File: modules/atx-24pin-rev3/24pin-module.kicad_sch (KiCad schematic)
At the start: 64 parts, among them J1 TO-HUB, J2 TO-HUB-PWR, J3 ATX-24 PSU, J4 ATX-24 MB, J5 USB-C 2.0, J6 TO-HUB-STACK, SW1 BOOT, SW2 RESET, U1 ESP32-C6-MINI-1-N4, U10 INA228, U11 INA228, U12 INA228, U13 INA228, U2 TJA1051T/3, U3 LP5907MFX-3.3, U5 TPS2121RUXR, U612V INA181A2IDBVR, U65V INA181A2IDBVR, U712V TLV7011DBVR, U75V TLV7011DBVR

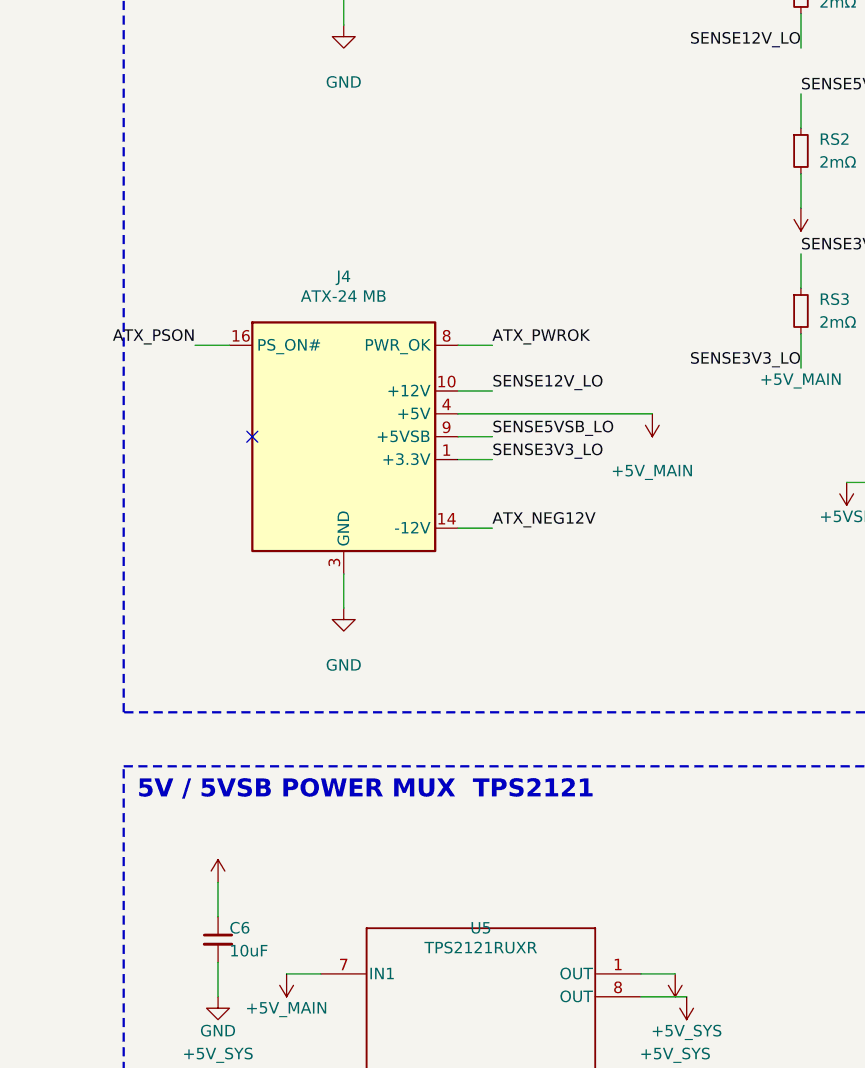
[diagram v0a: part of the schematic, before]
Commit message: Task 9: blade interface on main boards — J4/J_OUT* -> Keystone 3586 clips + J_SIG (SS2.8 v1.4.0)
24pin-rev3 hand-splice: TB1..TB9 per the ratified rail split + 2x5 J_SIG
(PS_ON#/PWR_OK/-12V/GND; pins 5-10 reserved — NO remote-sense net exists on
J4, verified not invented); EPS/PCIe = generator edits + regen (TB per-cable
3+3 / 2+2 on /SENSEC*_LO + GND). Modeled-delta assertions PASS all 4 boards
(exactly J_OUT/J4 out, TB/J_SIG in; inventory otherwise byte-identical);
ERC byte-identical on EPS/PCIe, 24pin +4 benign warnings/errors unchanged;
BOMs updated (C238113 in, Mini-Fit-out rows gone). Rev -> BETA-2. Two real
shared-code bugs fixed (auto_io vertical-pin heuristic; title_block comment4
arity). Sense-return NOT added (owner box (e) open — provision comments).
12VHPWR + all inputs untouched. 24pin pre-existing missing_lib_symbol x4 ->
FOLLOWUPS.

Co-Authored-By: Claude Fable 5 <noreply@anthropic.com>
Claude-Session: https://claude.ai/code/session_01LvfqcnEeuin2oyJQw548EX
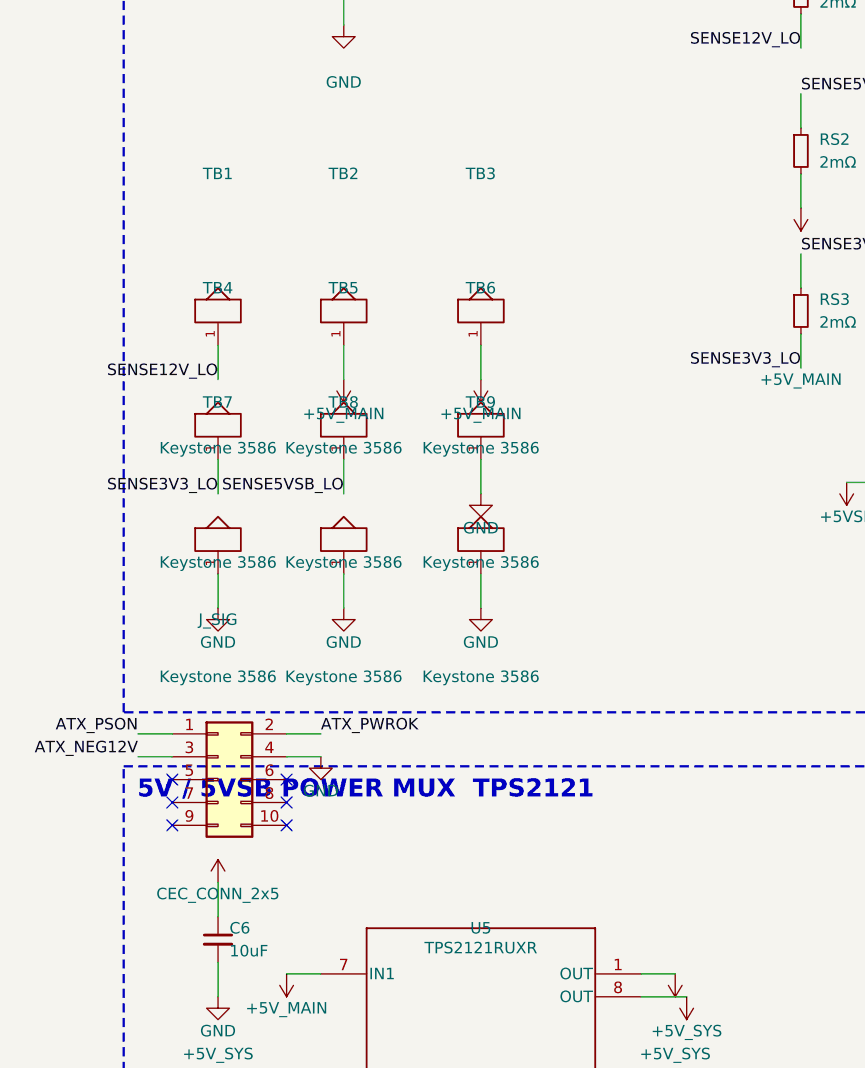
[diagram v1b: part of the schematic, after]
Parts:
- removed J4: ATX-24 MB, cec-Connector_Molex:Molex_Mini-Fit_Jr_5569-24A2_2x12_P4.20mm_Horizontal, symbol cec:CEC_ATX_24
- added J_SIG: CEC_CONN_2x5, cec-Connector_PinHeader_2.54mm:PinHeader_2x05_P2.54mm_Vertical, symbol cec:CEC_CONN_2x5
- added TB1, TB2, TB3, TB4, TB5, TB6, TB7, TB8, TB9: Keystone 3586, cec-Connector_Blade:Keystone_3586_SMD_Universal_Blade_Clip, symbol cec-vendor:Keystone_3586_Blade_Clip
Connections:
- net +3V3: now also J_SIG.4 (Pin_4), TB6.1, TB7.1, TB8.1, TB9.1
- net +5V_MAIN: now also TB2.1, TB3.1
- net ATX_NEG12V: now also J_SIG.3 (Pin_3)
- net ATX_PSON: now also J_SIG.1 (Pin_1)
- net ATX_PWROK: now also J_SIG.2 (Pin_2)
- net SENSE12V_LO: now also TB1.1
- net SENSE3V3_LO: now also TB4.1
- net SENSE5VSB_LO: now also TB5.1
- no-connect marks 34 -> 39

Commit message: WIP snapshot: INA238 ruling application in progress (spec v1.5.0 + 24pin-rev3 swap, verification pending; durability)
Co-Authored-By: Claude Fable 5 <noreply@anthropic.com>
Claude-Session: https://claude.ai/code/session_01LvfqcnEeuin2oyJQw548EX
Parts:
- U10, U11, U12, U13: value INA228 -> INA238; LCSC (none) -> C2868250; MPN (none) -> INA238AIDGSR; Manufacturer (none) -> Texas Instruments
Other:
- note added: "RAIL SENSING 4x INA238"
- note removed: "RAIL SENSING 4x INA228"
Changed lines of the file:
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@@
 		(fill (type none))
 	)
-	(text "RAIL SENSING  4x INA228"
+	(text "RAIL SENSING  4x INA238"
 		(exclude_from_sim no)
 		(at 135.5 25.5 0)
@@
 		(fields_autoplaced yes)
 		(property "Reference" "U10" (at 151.52 49.61 0) (effects (font (size 1.27 1.27)) (justify right)))
-		(property "Value" "INA228" (at 151.52 52.11 0) (effects (font (size 1.27 1.27)) (justify right)))
+		(property "Value" "INA238" (at 151.52 52.11 0) (effects (font (size 1.27 1.27)) (justify right)))
 		(property "Footprint" "cec-Package_SO:VSSOP-10_3x3mm_P0.5mm" (at 160.02 54.61 0) (effects (font (size 1.27 1.27)) (hide yes)))
 		(property "Datasheet" "" (at 160.02 54.61 0) (effects (font (size 1.27 1.27)) (hide yes)))
+		(property "Manufacturer" "Texas Instruments" (at 160.02 54.61 0) (effects (font (size 1.27 1.27)) (hide yes)))
+		(property "MPN" "INA238AIDGSR" (at 160.02 54.61 0) (effects (font (size 1.27 1.27)) (hide yes)))
+		(property "LCSC" "C2868250" (at 160.02 54.61 0) (effects (font (size 1.27 1.27)) (hide yes)))
 		(pin "8")
 		(pin "10")
@@
 		(fields_autoplaced yes)
 		(property "Reference" "U11" (at 150.25 80.09 0) (effects (font (size 1.27 1.27)) (justify right)))
-		(property "Value" "INA228" (at 150.25 82.29 0) (effects (font (size 1.27 1.27)) (justify right)))
+		(property "Value" "INA238" (at 150.25 82.29 0) (effects (font (size 1.27 1.27)) (justify right)))
 		(property "Footprint" "cec-Package_SO:VSSOP-10_3x3mm_P0.5mm" (at 160.02 85.09 0) (effects (font (size 1.27 1.27)) (hide yes)))
 		(property "Datasheet" "" (at 160.02 85.09 0) (effects (font (size 1.27 1.27)) (hide yes)))
+		(property "Manufacturer" "Texas Instruments" (at 160.02 85.09 0) (effects (font (size 1.27 1.27)) (hide yes)))
+		(property "MPN" "INA238AIDGSR" (at 160.02 85.09 0) (effects (font (size 1.27 1.27)) (hide yes)))
+		(property "LCSC" "C2868250" (at 160.02 85.09 0) (effects (font (size 1.27 1.27)) (hide yes)))
 		(pin "8")
 		(pin "10")
@@
 		(fields_autoplaced yes)
 		(property "Reference" "U12" (at 151.52 110.57 0) (effects (font (size 1.27 1.27)) (justify right)))
-		(property "Value" "INA228" (at 151.52 113.07 0) (effects (font (size 1.27 1.27)) (justify right)))
+		(property "Value" "INA238" (at 151.52 113.07 0) (effects (font (size 1.27 1.27)) (justify right)))
 		(property "Footprint" "cec-Package_SO:VSSOP-10_3x3mm_P0.5mm" (at 160.02 115.57 0) (effects (font (size 1.27 1.27)) (hide yes)))
 		(property "Datasheet" "" (at 160.02 115.57 0) (effects (font (size 1.27 1.27)) (hide yes)))
+		(property "Manufacturer" "Texas Instruments" (at 160.02 115.57 0) (effects (font (size 1.27 1.27)) (hide yes)))
+		(property "MPN" "INA238AIDGSR" (at 160.02 115.57 0) (effects (font (size 1.27 1.27)) (hide yes)))
+		(property "LCSC" "C2868250" (at 160.02 115.57 0) (effects (font (size 1.27 1.27)) (hide yes)))
 		(pin "8")
 		(pin "10")
@@
 		(fields_autoplaced yes)
 		(property "Reference" "U13" (at 201.05 49.61 0) (effects (font (size 1.27 1.27)) (justify right)))
-		(property "Value" "INA228" (at 201.05 51.81 0) (effects (font (size 1.27 1.27)) (justify right)))
+		(property "Value" "INA238" (at 201.05 51.81 0) (effects (font (size 1.27 1.27)) (justify right)))
 		(property "Footprint" "cec-Package_SO:VSSOP-10_3x3mm_P0.5mm" (at 209.55 54.61 0) (effects (font (size 1.27 1.27)) (hide yes)))
 		(property "Datasheet" "" (at 209.55 54.61 0) (effects (font (size 1.27 1.27)) (hide yes)))
+		(property "Manufacturer" "Texas Instruments" (at 209.55 54.61 0) (effects (font (size 1.27 1.27)) (hide yes)))
+		(property "MPN" "INA238AIDGSR" (at 209.55 54.61 0) (effects (font (size 1.27 1.27)) (hide yes)))
+		(property "LCSC" "C2868250" (at 209.55 54.61 0) (effects (font (size 1.27 1.27)) (hide yes)))
 		(pin "8")
 		(pin "10")

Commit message: WIP snapshot: iteration-5 main-board clip swap in flight (durability)
Co-Authored-By: Claude Fable 5 <noreply@anthropic.com>
Claude-Session: https://claude.ai/code/session_01LvfqcnEeuin2oyJQw548EX
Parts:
- TB1: value Keystone 3586 -> Keystone 3557; footprint cec-Connector_Blade:Keystone_3586_SMD_Universal_Blade_Clip -> cec-Connector_Blade:Keystone_3557_THT_Universal_Clip_TopEntry; LCSC C238113 -> C3205403; MPN 3586 -> 3557; Note Output daughterboard blade clip, ratified joint 12V (spec Sec 2.8 v1.4.0); mates with the TE 63849-1 tab on the daughterboard side. -> Output daughterboard blade clip, ratified joint 12V (spec Sec 2.8 v1.4.0); mates with the TE 63849-1 tab on the daughterboard side. [2026-07-05 iteration 5: clip part swapped Keystone 3586 (SMD) -> Keystone 3557 bare top-entry clip (THT, UL 30A@500VAC, catalog M55 p.41; LCSC carriage: 3557-10/C3205403 in the fuse-holder category, variant UNVERIFIED -- DigiKey/Mouser carry 3557 directly, consigned fallback; 3586 stays vendored as the SMD fallback pending the OQ-86 sample). Rotated: slot axis perpendicular to the daughterboard wall line, legs ALONG the clip row (3.4mm pitch, verified from the catalog mounting details). Mates the TE 63951-1 right-angle tab descending blade-down from the daughterboard -- see docs/standard-tier-review/blade-fit-check-2026-07-04.md addenda 3-5.]
- TB2: value Keystone 3586 -> Keystone 3557; footprint cec-Connector_Blade:Keystone_3586_SMD_Universal_Blade_Clip -> cec-Connector_Blade:Keystone_3557_THT_Universal_Clip_TopEntry; LCSC C238113 -> C3205403; MPN 3586 -> 3557; Note Output daughterboard blade clip, ratified joint 5V (1 of 2) (spec Sec 2.8 v1.4.0); mates with the TE 63849-1 tab on the daughterboard side. -> Output daughterboard blade clip, ratified joint 5V (1 of 2) (spec Sec 2.8 v1.4.0); mates with the TE 63849-1 tab on the daughterboard side. [2026-07-05 iteration 5: clip part swapped Keystone 3586 (SMD) -> Keystone 3557 bare top-entry clip (THT, UL 30A@500VAC, catalog M55 p.41; LCSC carriage: 3557-10/C3205403 in the fuse-holder category, variant UNVERIFIED -- DigiKey/Mouser carry 3557 directly, consigned fallback; 3586 stays vendored as the SMD fallback pending the OQ-86 sample). Rotated: slot axis perpendicular to the daughterboard wall line, legs ALONG the clip row (3.4mm pitch, verified from the catalog mounting details). Mates the TE 63951-1 right-angle tab descending blade-down from the daughterboard -- see docs/standard-tier-review/blade-fit-check-2026-07-04.md addenda 3-5.]
- TB3: value Keystone 3586 -> Keystone 3557; footprint cec-Connector_Blade:Keystone_3586_SMD_Universal_Blade_Clip -> cec-Connector_Blade:Keystone_3557_THT_Universal_Clip_TopEntry; LCSC C238113 -> C3205403; MPN 3586 -> 3557; Note Output daughterboard blade clip, ratified joint 5V (2 of 2) (spec Sec 2.8 v1.4.0); mates with the TE 63849-1 tab on the daughterboard side. -> Output daughterboard blade clip, ratified joint 5V (2 of 2) (spec Sec 2.8 v1.4.0); mates with the TE 63849-1 tab on the daughterboard side. [2026-07-05 iteration 5: clip part swapped Keystone 3586 (SMD) -> Keystone 3557 bare top-entry clip (THT, UL 30A@500VAC, catalog M55 p.41; LCSC carriage: 3557-10/C3205403 in the fuse-holder category, variant UNVERIFIED -- DigiKey/Mouser carry 3557 directly, consigned fallback; 3586 stays vendored as the SMD fallback pending the OQ-86 sample). Rotated: slot axis perpendicular to the daughterboard wall line, legs ALONG the clip row (3.4mm pitch, verified from the catalog mounting details). Mates the TE 63951-1 right-angle tab descending blade-down from the daughterboard -- see docs/standard-tier-review/blade-fit-check-2026-07-04.md addenda 3-5.]
- TB4: value Keystone 3586 -> Keystone 3557; footprint cec-Connector_Blade:Keystone_3586_SMD_Universal_Blade_Clip -> cec-Connector_Blade:Keystone_3557_THT_Universal_Clip_TopEntry; LCSC C238113 -> C3205403; MPN 3586 -> 3557; Note Output daughterboard blade clip, ratified joint 3.3V (spec Sec 2.8 v1.4.0); mates with the TE 63849-1 tab on the daughterboard side. -> Output daughterboard blade clip, ratified joint 3.3V (spec Sec 2.8 v1.4.0); mates with the TE 63849-1 tab on the daughterboard side. [2026-07-05 iteration 5: clip part swapped Keystone 3586 (SMD) -> Keystone 3557 bare top-entry clip (THT, UL 30A@500VAC, catalog M55 p.41; LCSC carriage: 3557-10/C3205403 in the fuse-holder category, variant UNVERIFIED -- DigiKey/Mouser carry 3557 directly, consigned fallback; 3586 stays vendored as the SMD fallback pending the OQ-86 sample). Rotated: slot axis perpendicular to the daughterboard wall line, legs ALONG the clip row (3.4mm pitch, verified from the catalog mounting details). Mates the TE 63951-1 right-angle tab descending blade-down from the daughterboard -- see docs/standard-tier-review/blade-fit-check-2026-07-04.md addenda 3-5.]
- TB5: value Keystone 3586 -> Keystone 3557; footprint cec-Connector_Blade:Keystone_3586_SMD_Universal_Blade_Clip -> cec-Connector_Blade:Keystone_3557_THT_Universal_Clip_TopEntry; LCSC C238113 -> C3205403; MPN 3586 -> 3557; Note Output daughterboard blade clip, ratified joint 5VSB (spec Sec 2.8 v1.4.0); mates with the TE 63849-1 tab on the daughterboard side. -> Output daughterboard blade clip, ratified joint 5VSB (spec Sec 2.8 v1.4.0); mates with the TE 63849-1 tab on the daughterboard side. [2026-07-05 iteration 5: clip part swapped Keystone 3586 (SMD) -> Keystone 3557 bare top-entry clip (THT, UL 30A@500VAC, catalog M55 p.41; LCSC carriage: 3557-10/C3205403 in the fuse-holder category, variant UNVERIFIED -- DigiKey/Mouser carry 3557 directly, consigned fallback; 3586 stays vendored as the SMD fallback pending the OQ-86 sample). Rotated: slot axis perpendicular to the daughterboard wall line, legs ALONG the clip row (3.4mm pitch, verified from the catalog mounting details). Mates the TE 63951-1 right-angle tab descending blade-down from the daughterboard -- see docs/standard-tier-review/blade-fit-check-2026-07-04.md addenda 3-5.]
- TB6: value Keystone 3586 -> Keystone 3557; footprint cec-Connector_Blade:Keystone_3586_SMD_Universal_Blade_Clip -> cec-Connector_Blade:Keystone_3557_THT_Universal_Clip_TopEntry; LCSC C238113 -> C3205403; MPN 3586 -> 3557; Note Output daughterboard blade clip, ratified joint GND (1 of 4) (spec Sec 2.8 v1.4.0); mates with the TE 63849-1 tab on the daughterboard side. -> Output daughterboard blade clip, ratified joint GND (1 of 4) (spec Sec 2.8 v1.4.0); mates with the TE 63849-1 tab on the daughterboard side. [2026-07-05 iteration 5: clip part swapped Keystone 3586 (SMD) -> Keystone 3557 bare top-entry clip (THT, UL 30A@500VAC, catalog M55 p.41; LCSC carriage: 3557-10/C3205403 in the fuse-holder category, variant UNVERIFIED -- DigiKey/Mouser carry 3557 directly, consigned fallback; 3586 stays vendored as the SMD fallback pending the OQ-86 sample). Rotated: slot axis perpendicular to the daughterboard wall line, legs ALONG the clip row (3.4mm pitch, verified from the catalog mounting details). Mates the TE 63951-1 right-angle tab descending blade-down from the daughterboard -- see docs/standard-tier-review/blade-fit-check-2026-07-04.md addenda 3-5.]
- TB7: value Keystone 3586 -> Keystone 3557; footprint cec-Connector_Blade:Keystone_3586_SMD_Universal_Blade_Clip -> cec-Connector_Blade:Keystone_3557_THT_Universal_Clip_TopEntry; LCSC C238113 -> C3205403; MPN 3586 -> 3557; Note Output daughterboard blade clip, ratified joint GND (2 of 4) (spec Sec 2.8 v1.4.0); mates with the TE 63849-1 tab on the daughterboard side. -> Output daughterboard blade clip, ratified joint GND (2 of 4) (spec Sec 2.8 v1.4.0); mates with the TE 63849-1 tab on the daughterboard side. [2026-07-05 iteration 5: clip part swapped Keystone 3586 (SMD) -> Keystone 3557 bare top-entry clip (THT, UL 30A@500VAC, catalog M55 p.41; LCSC carriage: 3557-10/C3205403 in the fuse-holder category, variant UNVERIFIED -- DigiKey/Mouser carry 3557 directly, consigned fallback; 3586 stays vendored as the SMD fallback pending the OQ-86 sample). Rotated: slot axis perpendicular to the daughterboard wall line, legs ALONG the clip row (3.4mm pitch, verified from the catalog mounting details). Mates the TE 63951-1 right-angle tab descending blade-down from the daughterboard -- see docs/standard-tier-review/blade-fit-check-2026-07-04.md addenda 3-5.]
- TB8: value Keystone 3586 -> Keystone 3557; footprint cec-Connector_Blade:Keystone_3586_SMD_Universal_Blade_Clip -> cec-Connector_Blade:Keystone_3557_THT_Universal_Clip_TopEntry; LCSC C238113 -> C3205403; MPN 3586 -> 3557; Note Output daughterboard blade clip, ratified joint GND (3 of 4) (spec Sec 2.8 v1.4.0); mates with the TE 63849-1 tab on the daughterboard side. -> Output daughterboard blade clip, ratified joint GND (3 of 4) (spec Sec 2.8 v1.4.0); mates with the TE 63849-1 tab on the daughterboard side. [2026-07-05 iteration 5: clip part swapped Keystone 3586 (SMD) -> Keystone 3557 bare top-entry clip (THT, UL 30A@500VAC, catalog M55 p.41; LCSC carriage: 3557-10/C3205403 in the fuse-holder category, variant UNVERIFIED -- DigiKey/Mouser carry 3557 directly, consigned fallback; 3586 stays vendored as the SMD fallback pending the OQ-86 sample). Rotated: slot axis perpendicular to the daughterboard wall line, legs ALONG the clip row (3.4mm pitch, verified from the catalog mounting details). Mates the TE 63951-1 right-angle tab descending blade-down from the daughterboard -- see docs/standard-tier-review/blade-fit-check-2026-07-04.md addenda 3-5.]
- TB9: value Keystone 3586 -> Keystone 3557; footprint cec-Connector_Blade:Keystone_3586_SMD_Universal_Blade_Clip -> cec-Connector_Blade:Keystone_3557_THT_Universal_Clip_TopEntry; LCSC C238113 -> C3205403; MPN 3586 -> 3557; Note Output daughterboard blade clip, ratified joint GND (4 of 4) (spec Sec 2.8 v1.4.0); mates with the TE 63849-1 tab on the daughterboard side. -> Output daughterboard blade clip, ratified joint GND (4 of 4) (spec Sec 2.8 v1.4.0); mates with the TE 63849-1 tab on the daughterboard side. [2026-07-05 iteration 5: clip part swapped Keystone 3586 (SMD) -> Keystone 3557 bare top-entry clip (THT, UL 30A@500VAC, catalog M55 p.41; LCSC carriage: 3557-10/C3205403 in the fuse-holder category, variant UNVERIFIED -- DigiKey/Mouser carry 3557 directly, consigned fallback; 3586 stays vendored as the SMD fallback pending the OQ-86 sample). Rotated: slot axis perpendicular to the daughterboard wall line, legs ALONG the clip row (3.4mm pitch, verified from the catalog mounting details). Mates the TE 63951-1 right-angle tab descending blade-down from the daughterboard -- see docs/standard-tier-review/blade-fit-check-2026-07-04.md addenda 3-5.]

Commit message: Daughterboard iteration 7 LANDED: TE 63969-1 receptacles, owner-ratified counts, orientation checker-proven
- Boards: atx24 61.0x21.4 @4.2mm/10 tabs; eps 28.5x20.0 @4.7/6; pcie 31.0x20.0 @5.2/6 (grows: +2 ratified joints outweigh the pitch win — honest number)
- Orientation proven from the rev-E drawing (memo addendum 7 F.1) + structural checker assertion (hole pair perpendicular to row, plan-congruent with the blade's leg holes, per position)
- atx24 rail allocation at 18.32A/joint: 12V 1 / 5V 2 / 3V3 2 (the gained joint; was 95% FAIL) / 5VSB 1 / GND 4 @127.2% hairline — honest 10
- Receptacle depth un-dimensioned on rev E: sample-gated 3.4-3.7 est w/ explicit >4.0mm => atx24-falls-back-to-6.3 gate in the checker
- Main boards: TB property swaps to TE 63969-1/C2961150 + ratified adds netlist-verified post-shunt (24pin TB10, pcie +2/cable); STALE Keystone-3586 BOM lines from Task 9 fixed
- Coordinator re-verified: ERC 0 x3 + DRC 0/0 x3 daughterboards; checker 113 OKs; 24pin-rev3 ERC = 1 pre-existing pin_not_driven only
- New sample items: detent hole ~0.5mm above receptacle top (retention friction-only?), gang insertion <=26N LIF / <=44N std per joint

Co-Authored-By: Claude Fable 5 <noreply@anthropic.com>
Claude-Session: https://claude.ai/code/session_01LvfqcnEeuin2oyJQw548EX
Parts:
- added TB10: TE 63969-1, cec-Connector_Blade:TE_63969_FASTON_Receptacle_250_Vertical_THT, symbol cec-vendor:Keystone_3586_Blade_Clip
- TB1: value Keystone 3557 -> TE 63969-1; footprint cec-Connector_Blade:Keystone_3557_THT_Universal_Clip_TopEntry -> cec-Connector_Blade:TE_63969_FASTON_Receptacle_250_Vertical_THT; LCSC C3205403 -> C2961150; MPN 3557 -> 63969-1; Manufacturer Keystone Electronics Corp. -> TE Connectivity; Note Output daughterboard blade clip, ratified joint 12V (spec Sec 2.8 v1.4.0); mates with the TE 63849-1 tab on the daughterboard side. [2026-07-05 iteration 5: clip part swapped Keystone 3586 (SMD) -> Keystone 3557 bare top-entry clip (THT, UL 30A@500VAC, catalog M55 p.41; LCSC carriage: 3557-10/C3205403 in the fuse-holder category, variant UNVERIFIED -- DigiKey/Mouser carry 3557 directly, consigned fallback; 3586 stays vendored as the SMD fallback pending the OQ-86 sample). Rotated: slot axis perpendicular to the daughterboard wall line, legs ALONG the clip row (3.4mm pitch, verified from the catalog mounting details). Mates the TE 63951-1 right-angle tab descending blade-down from the daughterboard -- see docs/standard-tier-review/blade-fit-check-2026-07-04.md addenda 3-5.] -> Output daughterboard blade clip, ratified joint 12V (spec Sec 2.8 v1.4.0); mates with the TE 63849-1 tab on the daughterboard side. [2026-07-05 iteration 5: clip part swapped Keystone 3586 (SMD) -> Keystone 3557 bare top-entry clip (THT, UL 30A@500VAC, catalog M55 p.41; LCSC carriage: 3557-10/C3205403 in the fuse-holder category, variant UNVERIFIED -- DigiKey/Mouser carry 3557 directly, consigned fallback; 3586 stays vendored as the SMD fallback pending the OQ-86 sample). Rotated: slot axis perpendicular to the daughterboard wall line, legs ALONG the clip row (3.4mm pitch, verified from the catalog mounting details). Mates the TE 63951-1 right-angle tab descending blade-down from the daughterboard -- see docs/standard-tier-review/blade-fit-check-2026-07-04.md addenda 3-5.] [2026-07-06 iteration 7: mate swapped Keystone 3557 -> TE 63969-1 FASTON .250 PCB receptacle (owner-ratified; the DESIGNED mate for the 63951-1 blade -- 0.81mm thickness at its design centre per rev-E dwg note 3, ve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
- TB2: value Keystone 3557 -> TE 63969-1; footprint cec-Connector_Blade:Keystone_3557_THT_Universal_Clip_TopEntry -> cec-Connector_Blade:TE_63969_FASTON_Receptacle_250_Vertical_THT; LCSC C3205403 -> C2961150; MPN 3557 -> 63969-1; Manufacturer Keystone Electronics Corp. -> TE Connectivity; Note Output daughterboard blade clip, ratified joint 5V (1 of 2) (spec Sec 2.8 v1.4.0); mates with the TE 63849-1 tab on the daughterboard side. [2026-07-05 iteration 5: clip part swapped Keystone 3586 (SMD) -> Keystone 3557 bare top-entry clip (THT, UL 30A@500VAC, catalog M55 p.41; LCSC carriage: 3557-10/C3205403 in the fuse-holder category, variant UNVERIFIED -- DigiKey/Mouser carry 3557 directly, consigned fallback; 3586 stays vendored as the SMD fallback pending the OQ-86 sample). Rotated: slot axis perpendicular to the daughterboard wall line, legs ALONG the clip row (3.4mm pitch, verified from the catalog mounting details). Mates the TE 63951-1 right-angle tab descending blade-down from the daughterboard -- see docs/standard-tier-review/blade-fit-check-2026-07-04.md addenda 3-5.] -> Output daughterboard blade clip, ratified joint 5V (1 of 2) (spec Sec 2.8 v1.4.0); mates with the TE 63849-1 tab on the daughterboard side. [2026-07-05 iteration 5: clip part swapped Keystone 3586 (SMD) -> Keystone 3557 bare top-entry clip (THT, UL 30A@500VAC, catalog M55 p.41; LCSC carriage: 3557-10/C3205403 in the fuse-holder category, variant UNVERIFIED -- DigiKey/Mouser carry 3557 directly, consigned fallback; 3586 stays vendored as the SMD fallback pending the OQ-86 sample). Rotated: slot axis perpendicular to the daughterboard wall line, legs ALONG the clip row (3.4mm pitch, verified from the catalog mounting details). Mates the TE 63951-1 right-angle tab descending blade-down from the daughterboard -- see docs/standard-tier-review/blade-fit-check-2026-07-04.md addenda 3-5.] [2026-07-06 iteration 7: mate swapped Keystone 3557 -> TE 63969-1 FASTON .250 PCB receptacle (owner-ratified; the DESIGNED mate for the 63951-1 blade -- 0.81mm thickness at its design centre per rev-E dwg no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
- TB3: value Keystone 3557 -> TE 63969-1; footprint cec-Connector_Blade:Keystone_3557_THT_Universal_Clip_TopEntry -> cec-Connector_Blade:TE_63969_FASTON_Receptacle_250_Vertical_THT; LCSC C3205403 -> C2961150; MPN 3557 -> 63969-1; Manufacturer Keystone Electronics Corp. -> TE Connectivity; Note Output daughterboard blade clip, ratified joint 5V (2 of 2) (spec Sec 2.8 v1.4.0); mates with the TE 63849-1 tab on the daughterboard side. [2026-07-05 iteration 5: clip part swapped Keystone 3586 (SMD) -> Keystone 3557 bare top-entry clip (THT, UL 30A@500VAC, catalog M55 p.41; LCSC carriage: 3557-10/C3205403 in the fuse-holder category, variant UNVERIFIED -- DigiKey/Mouser carry 3557 directly, consigned fallback; 3586 stays vendored as the SMD fallback pending the OQ-86 sample). Rotated: slot axis perpendicular to the daughterboard wall line, legs ALONG the clip row (3.4mm pitch, verified from the catalog mounting details). Mates the TE 63951-1 right-angle tab descending blade-down from the daughterboard -- see docs/standard-tier-review/blade-fit-check-2026-07-04.md addenda 3-5.] -> Output daughterboard blade clip, ratified joint 5V (2 of 2) (spec Sec 2.8 v1.4.0); mates with the TE 63849-1 tab on the daughterboard side. [2026-07-05 iteration 5: clip part swapped Keystone 3586 (SMD) -> Keystone 3557 bare top-entry clip (THT, UL 30A@500VAC, catalog M55 p.41; LCSC carriage: 3557-10/C3205403 in the fuse-holder category, variant UNVERIFIED -- DigiKey/Mouser carry 3557 directly, consigned fallback; 3586 stays vendored as the SMD fallback pending the OQ-86 sample). Rotated: slot axis perpendicular to the daughterboard wall line, legs ALONG the clip row (3.4mm pitch, verified from the catalog mounting details). Mates the TE 63951-1 right-angle tab descending blade-down from the daughterboard -- see docs/standard-tier-review/blade-fit-check-2026-07-04.md addenda 3-5.] [2026-07-06 iteration 7: mate swapped Keystone 3557 -> TE 63969-1 FASTON .250 PCB receptacle (owner-ratified; the DESIGNED mate for the 63951-1 blade -- 0.81mm thickness at its design centre per rev-E dwg no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
- TB4: value Keystone 3557 -> TE 63969-1; footprint cec-Connector_Blade:Keystone_3557_THT_Universal_Clip_TopEntry -> cec-Connector_Blade:TE_63969_FASTON_Receptacle_250_Vertical_THT; LCSC C3205403 -> C2961150; MPN 3557 -> 63969-1; Manufacturer Keystone Electronics Corp. -> TE Connectivity; Note Output daughterboard blade clip, ratified joint 3.3V (spec Sec 2.8 v1.4.0); mates with the TE 63849-1 tab on the daughterboard side. [2026-07-05 iteration 5: clip part swapped Keystone 3586 (SMD) -> Keystone 3557 bare top-entry clip (THT, UL 30A@500VAC, catalog M55 p.41; LCSC carriage: 3557-10/C3205403 in the fuse-holder category, variant UNVERIFIED -- DigiKey/Mouser carry 3557 directly, consigned fallback; 3586 stays vendored as the SMD fallback pending the OQ-86 sample). Rotated: slot axis perpendicular to the daughterboard wall line, legs ALONG the clip row (3.4mm pitch, verified from the catalog mounting details). Mates the TE 63951-1 right-angle tab descending blade-down from the daughterboard -- see docs/standard-tier-review/blade-fit-check-2026-07-04.md addenda 3-5.] -> Output daughterboard blade clip, ratified joint 3.3V (spec Sec 2.8 v1.4.0); mates with the TE 63849-1 tab on the daughterboard side. [2026-07-05 iteration 5: clip part swapped Keystone 3586 (SMD) -> Keystone 3557 bare top-entry clip (THT, UL 30A@500VAC, catalog M55 p.41; LCSC carriage: 3557-10/C3205403 in the fuse-holder category, variant UNVERIFIED -- DigiKey/Mouser carry 3557 directly, consigned fallback; 3586 stays vendored as the SMD fallback pending the OQ-86 sample). Rotated: slot axis perpendicular to the daughterboard wall line, legs ALONG the clip row (3.4mm pitch, verified from the catalog mounting details). Mates the TE 63951-1 right-angle tab descending blade-down from the daughterboard -- see docs/standard-tier-review/blade-fit-check-2026-07-04.md addenda 3-5.] [2026-07-06 iteration 7: mate swapped Keystone 3557 -> TE 63969-1 FASTON .250 PCB receptacle (owner-ratified; the DESIGNED mate for the 63951-1 blade -- 0.81mm thickness at its design centre per rev-E dwg note 3, v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
- TB5: value Keystone 3557 -> TE 63969-1; footprint cec-Connector_Blade:Keystone_3557_THT_Universal_Clip_TopEntry -> cec-Connector_Blade:TE_63969_FASTON_Receptacle_250_Vertical_THT; LCSC C3205403 -> C2961150; MPN 3557 -> 63969-1; Manufacturer Keystone Electronics Corp. -> TE Connectivity; Note Output daughterboard blade clip, ratified joint 5VSB (spec Sec 2.8 v1.4.0); mates with the TE 63849-1 tab on the daughterboard side. [2026-07-05 iteration 5: clip part swapped Keystone 3586 (SMD) -> Keystone 3557 bare top-entry clip (THT, UL 30A@500VAC, catalog M55 p.41; LCSC carriage: 3557-10/C3205403 in the fuse-holder category, variant UNVERIFIED -- DigiKey/Mouser carry 3557 directly, consigned fallback; 3586 stays vendored as the SMD fallback pending the OQ-86 sample). Rotated: slot axis perpendicular to the daughterboard wall line, legs ALONG the clip row (3.4mm pitch, verified from the catalog mounting details). Mates the TE 63951-1 right-angle tab descending blade-down from the daughterboard -- see docs/standard-tier-review/blade-fit-check-2026-07-04.md addenda 3-5.] -> Output daughterboard blade clip, ratified joint 5VSB (spec Sec 2.8 v1.4.0); mates with the TE 63849-1 tab on the daughterboard side. [2026-07-05 iteration 5: clip part swapped Keystone 3586 (SMD) -> Keystone 3557 bare top-entry clip (THT, UL 30A@500VAC, catalog M55 p.41; LCSC carriage: 3557-10/C3205403 in the fuse-holder category, variant UNVERIFIED -- DigiKey/Mouser carry 3557 directly, consigned fallback; 3586 stays vendored as the SMD fallback pending the OQ-86 sample). Rotated: slot axis perpendicular to the daughterboard wall line, legs ALONG the clip row (3.4mm pitch, verified from the catalog mounting details). Mates the TE 63951-1 right-angle tab descending blade-down from the daughterboard -- see docs/standard-tier-review/blade-fit-check-2026-07-04.md addenda 3-5.] [2026-07-06 iteration 7: mate swapped Keystone 3557 -> TE 63969-1 FASTON .250 PCB receptacle (owner-ratified; the DESIGNED mate for the 63951-1 blade -- 0.81mm thickness at its design centre per rev-E dwg note 3, v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
- TB6: value Keystone 3557 -> TE 63969-1; footprint cec-Connector_Blade:Keystone_3557_THT_Universal_Clip_TopEntry -> cec-Connector_Blade:TE_63969_FASTON_Receptacle_250_Vertical_THT; LCSC C3205403 -> C2961150; MPN 3557 -> 63969-1; Manufacturer Keystone Electronics Corp. -> TE Connectivity; Note Output daughterboard blade clip, ratified joint GND (1 of 4) (spec Sec 2.8 v1.4.0); mates with the TE 63849-1 tab on the daughterboard side. [2026-07-05 iteration 5: clip part swapped Keystone 3586 (SMD) -> Keystone 3557 bare top-entry clip (THT, UL 30A@500VAC, catalog M55 p.41; LCSC carriage: 3557-10/C3205403 in the fuse-holder category, variant UNVERIFIED -- DigiKey/Mouser carry 3557 directly, consigned fallback; 3586 stays vendored as the SMD fallback pending the OQ-86 sample). Rotated: slot axis perpendicular to the daughterboard wall line, legs ALONG the clip row (3.4mm pitch, verified from the catalog mounting details). Mates the TE 63951-1 right-angle tab descending blade-down from the daughterboard -- see docs/standard-tier-review/blade-fit-check-2026-07-04.md addenda 3-5.] -> Output daughterboard blade clip, ratified joint GND (1 of 4) (spec Sec 2.8 v1.4.0); mates with the TE 63849-1 tab on the daughterboard side. [2026-07-05 iteration 5: clip part swapped Keystone 3586 (SMD) -> Keystone 3557 bare top-entry clip (THT, UL 30A@500VAC, catalog M55 p.41; LCSC carriage: 3557-10/C3205403 in the fuse-holder category, variant UNVERIFIED -- DigiKey/Mouser carry 3557 directly, consigned fallback; 3586 stays vendored as the SMD fallback pending the OQ-86 sample). Rotated: slot axis perpendicular to the daughterboard wall line, legs ALONG the clip row (3.4mm pitch, verified from the catalog mounting details). Mates the TE 63951-1 right-angle tab descending blade-down from the daughterboard -- see docs/standard-tier-review/blade-fit-check-2026-07-04.md addenda 3-5.] [2026-07-06 iteration 7: mate swapped Keystone 3557 -> TE 63969-1 FASTON .250 PCB receptacle (owner-ratified; the DESIGNED mate for the 63951-1 blade -- 0.81mm thickness at its design centre per rev-E dwg n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
- TB7: value Keystone 3557 -> TE 63969-1; footprint cec-Connector_Blade:Keystone_3557_THT_Universal_Clip_TopEntry -> cec-Connector_Blade:TE_63969_FASTON_Receptacle_250_Vertical_THT; LCSC C3205403 -> C2961150; MPN 3557 -> 63969-1; Manufacturer Keystone Electronics Corp. -> TE Connectivity; Note Output daughterboard blade clip, ratified joint GND (2 of 4) (spec Sec 2.8 v1.4.0); mates with the TE 63849-1 tab on the daughterboard side. [2026-07-05 iteration 5: clip part swapped Keystone 3586 (SMD) -> Keystone 3557 bare top-entry clip (THT, UL 30A@500VAC, catalog M55 p.41; LCSC carriage: 3557-10/C3205403 in the fuse-holder category, variant UNVERIFIED -- DigiKey/Mouser carry 3557 directly, consigned fallback; 3586 stays vendored as the SMD fallback pending the OQ-86 sample). Rotated: slot axis perpendicular to the daughterboard wall line, legs ALONG the clip row (3.4mm pitch, verified from the catalog mounting details). Mates the TE 63951-1 right-angle tab descending blade-down from the daughterboard -- see docs/standard-tier-review/blade-fit-check-2026-07-04.md addenda 3-5.] -> Output daughterboard blade clip, ratified joint GND (2 of 4) (spec Sec 2.8 v1.4.0); mates with the TE 63849-1 tab on the daughterboard side. [2026-07-05 iteration 5: clip part swapped Keystone 3586 (SMD) -> Keystone 3557 bare top-entry clip (THT, UL 30A@500VAC, catalog M55 p.41; LCSC carriage: 3557-10/C3205403 in the fuse-holder category, variant UNVERIFIED -- DigiKey/Mouser carry 3557 directly, consigned fallback; 3586 stays vendored as the SMD fallback pending the OQ-86 sample). Rotated: slot axis perpendicular to the daughterboard wall line, legs ALONG the clip row (3.4mm pitch, verified from the catalog mounting details). Mates the TE 63951-1 right-angle tab descending blade-down from the daughterboard -- see docs/standard-tier-review/blade-fit-check-2026-07-04.md addenda 3-5.] [2026-07-06 iteration 7: mate swapped Keystone 3557 -> TE 63969-1 FASTON .250 PCB receptacle (owner-ratified; the DESIGNED mate for the 63951-1 blade -- 0.81mm thickness at its design centre per rev-E dwg n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
- TB8: value Keystone 3557 -> TE 63969-1; footprint cec-Connector_Blade:Keystone_3557_THT_Universal_Clip_TopEntry -> cec-Connector_Blade:TE_63969_FASTON_Receptacle_250_Vertical_THT; LCSC C3205403 -> C2961150; MPN 3557 -> 63969-1; Manufacturer Keystone Electronics Corp. -> TE Connectivity; Note Output daughterboard blade clip, ratified joint GND (3 of 4) (spec Sec 2.8 v1.4.0); mates with the TE 63849-1 tab on the daughterboard side. [2026-07-05 iteration 5: clip part swapped Keystone 3586 (SMD) -> Keystone 3557 bare top-entry clip (THT, UL 30A@500VAC, catalog M55 p.41; LCSC carriage: 3557-10/C3205403 in the fuse-holder category, variant UNVERIFIED -- DigiKey/Mouser carry 3557 directly, consigned fallback; 3586 stays vendored as the SMD fallback pending the OQ-86 sample). Rotated: slot axis perpendicular to the daughterboard wall line, legs ALONG the clip row (3.4mm pitch, verified from the catalog mounting details). Mates the TE 63951-1 right-angle tab descending blade-down from the daughterboard -- see docs/standard-tier-review/blade-fit-check-2026-07-04.md addenda 3-5.] -> Output daughterboard blade clip, ratified joint GND (3 of 4) (spec Sec 2.8 v1.4.0); mates with the TE 63849-1 tab on the daughterboard side. [2026-07-05 iteration 5: clip part swapped Keystone 3586 (SMD) -> Keystone 3557 bare top-entry clip (THT, UL 30A@500VAC, catalog M55 p.41; LCSC carriage: 3557-10/C3205403 in the fuse-holder category, variant UNVERIFIED -- DigiKey/Mouser carry 3557 directly, consigned fallback; 3586 stays vendored as the SMD fallback pending the OQ-86 sample). Rotated: slot axis perpendicular to the daughterboard wall line, legs ALONG the clip row (3.4mm pitch, verified from the catalog mounting details). Mates the TE 63951-1 right-angle tab descending blade-down from the daughterboard -- see docs/standard-tier-review/blade-fit-check-2026-07-04.md addenda 3-5.] [2026-07-06 iteration 7: mate swapped Keystone 3557 -> TE 63969-1 FASTON .250 PCB receptacle (owner-ratified; the DESIGNED mate for the 63951-1 blade -- 0.81mm thickness at its design centre per rev-E dwg n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
- TB9: value Keystone 3557 -> TE 63969-1; footprint cec-Connector_Blade:Keystone_3557_THT_Universal_Clip_TopEntry -> cec-Connector_Blade:TE_63969_FASTON_Receptacle_250_Vertical_THT; LCSC C3205403 -> C2961150; MPN 3557 -> 63969-1; Manufacturer Keystone Electronics Corp. -> TE Connectivity; Note Output daughterboard blade clip, ratified joint GND (4 of 4) (spec Sec 2.8 v1.4.0); mates with the TE 63849-1 tab on the daughterboard side. [2026-07-05 iteration 5: clip part swapped Keystone 3586 (SMD) -> Keystone 3557 bare top-entry clip (THT, UL 30A@500VAC, catalog M55 p.41; LCSC carriage: 3557-10/C3205403 in the fuse-holder category, variant UNVERIFIED -- DigiKey/Mouser carry 3557 directly, consigned fallback; 3586 stays vendored as the SMD fallback pending the OQ-86 sample). Rotated: slot axis perpendicular to the daughterboard wall line, legs ALONG the clip row (3.4mm pitch, verified from the catalog mounting details). Mates the TE 63951-1 right-angle tab descending blade-down from the daughterboard -- see docs/standard-tier-review/blade-fit-check-2026-07-04.md addenda 3-5.] -> Output daughterboard blade clip, ratified joint GND (4 of 4) (spec Sec 2.8 v1.4.0); mates with the TE 63849-1 tab on the daughterboard side. [2026-07-05 iteration 5: clip part swapped Keystone 3586 (SMD) -> Keystone 3557 bare top-entry clip (THT, UL 30A@500VAC, catalog M55 p.41; LCSC carriage: 3557-10/C3205403 in the fuse-holder category, variant UNVERIFIED -- DigiKey/Mouser carry 3557 directly, consigned fallback; 3586 stays vendored as the SMD fallback pending the OQ-86 sample). Rotated: slot axis perpendicular to the daughterboard wall line, legs ALONG the clip row (3.4mm pitch, verified from the catalog mounting details). Mates the TE 63951-1 right-angle tab descending blade-down from the daughterboard -- see docs/standard-tier-review/blade-fit-check-2026-07-04.md addenda 3-5.] [2026-07-06 iteration 7: mate swapped Keystone 3557 -> TE 63969-1 FASTON .250 PCB receptacle (owner-ratified; the DESIGNED mate for the 63951-1 blade -- 0.81mm thickness at its design centre per rev-E dwg n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
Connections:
- net SENSE3V3_LO: now also TB10.1
